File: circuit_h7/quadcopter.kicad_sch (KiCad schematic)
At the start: 143 parts, among them J1 Conn_01x01_Female, J10 Conn_01x01_Female, J11 Conn_01x04_Male, J12 Conn_01x04_Male, J13 Conn_01x01_Female, J14 Conn_01x01_Female, J15 Conn_01x01_Female, J16 Conn_01x01_Female, J17 Conn_01x01_Female, J18 USB_C_Receptacle_USB2.0, J19 Conn_01x08_Male, J2 Conn_01x01_Female, J20 Conn_01x01_Female, J21 Conn_01x01_Female, J22 Conn_01x01_Female, J23 Conn_01x01_Female, J24 Conn_01x01_Female, J25 Conn_01x01_Female, J26 Conn_01x01_Female, J28 Conn_01x01_Female, J29 Conn_01x01_Female, J3 Conn_01x01_Female, J30 Conn_01x01_Female, J31 Conn_01x01_Female, J32 Conn_01x01_Female, J33 Conn_01x01_Female, J37 Conn_01x01_Female, J4 Conn_01x01_Female, J40 Conn_01x01_Female, J41 Conn_01x01_Female, J42 Conn_01x01_Female, J43 Conn_01x01_Female, J44 Conn_01x01_Female, J45 Conn_01x01_Female, J47 Conn_01x01_Female, J48 Conn_01x01_Female, J49 Conn_01x01_Female, J5 Conn_Coaxial, J50 Conn_01x01_Female, J6 Conn_01x06_Male, J7 Conn_01x01_Female, J8 Conn_01x01_Female, J9 Conn_01x01_Female, Q1 AO3400A, SW1 SW_DIP_x01, U1 STM32H723VGH6, U10 ESP8285, U11 AMS1117-5.0, U12 TPS5430DDA, U13 5v, 3A, U2 ICM-42605, U3 DPS310, U4 3V3, U5 EUP3458 1.2A, 30V max input, 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, U6 2450FM07D0034T, U7 W25Q80DVUXIE TR (16M), U8 SX1281, U9 5v, 500mA, Y1 16M, Y2 52Mhz, 12pF, Y3 40M

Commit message: More work on H7 board
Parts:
- removed C21: 10nF 50V, Capacitor_SMD:C_0402_1005Metric, symbol Device:C
- removed C22: 2.2u, Capacitor_SMD:C_0402_1005Metric, symbol Device:C
- removed C24: 47uF 16V, Capacitor_SMD:C_1210_3225Metric, symbol Device:C
- removed C27: 22u 35v, Capacitor_SMD:C_0805_2012Metric, symbol Device:C
- removed C42: 150p, Capacitor_SMD:C_0402_1005Metric, symbol Device:C
- removed C43: 100n, Capacitor_SMD:C_0402_1005Metric, symbol Device:C
- removed C44: 1.5n, Capacitor_SMD:C_0402_1005Metric, symbol Device:C
- removed C45, C46: 10u, Capacitor_SMD:C_0805_2012Metric, symbol Device:C
- removed D2: 40v 1A B5819WS, Diode_SMD:D_SOD-323, symbol Device:D
- removed L4: 22u 900mA, Anyleaf_Shared:SMNR4020 inductor, symbol Device:L
- removed R17: 300, Resistor_SMD:R_0402_1005Metric, symbol Device:R
- removed R19: 10k, Resistor_SMD:R_0402_1005Metric, symbol Device:R
- removed U11: AMS1117-5.0, Package_TO_SOT_SMD:SOT-223-3_TabPin2, symbol Regulator_Linear:AMS1117-5.0
- removed U13: 5v, 3A, Package_DFN_QFN:DFN-10-1EP_3x3mm_P0.5mm_EP1.65x2.38mm, symbol water_monitor-rescue:MCP1802-3.3-Anyleaf_shared
- removed U5: EUP3458 1.2A, 30V max input, adj output, Package_TO_SOT_SMD:TSOT-23-6, symbol Regulator_Switching:AAT1217ICA-1.2
- removed U9: 5v, 500mA, Package_TO_SOT_SMD:TSOT-23-5, symbol water_monitor-rescue:MCP1802-3.3-Anyleaf_shared
- added J27, J34, J35, J36: Conn_01x01_Female, TestPoint:TestPoint_Pad_1.0x1.0mm, symbol Connector:Conn_01x01_Female
- added U5: MT2492 600kHz 16v 2A, Package_TO_SOT_SMD:SOT-23-6, symbol Regulator_Switching:TPS5430DDA
- C14: value 10uF 50V -> 22uF 25v; LCSC C440198 -> C602037; now in the parts list
- C15: value 1u 50V -> 22n; footprint Capacitor_SMD:C_0603_1608Metric -> Capacitor_SMD:C_0402_1005Metric; LCSC C15849 -> C1532; now in the parts list
- C20: value 47uF 16V -> 100uF 6.3V; footprint Capacitor_SMD:C_1210_3225Metric -> Capacitor_SMD:C_1206_3216Metric; LCSC C412625 -> C15008; now in the parts list
- J12: now left out of the parts list
- J3, J31, J37: footprint TestPoint:TestPoint_Pad_1.5x1.5mm -> TestPoint:TestPoint_Pad_2.0x2.0mm
- L2: value 100u 450mA -> 10u 2A; footprint Anyleaf_Shared:SMNR4020 inductor -> Inductor_SMD:L_Taiyo-Yuden_MD-4040; LCSC C467068 -> C98364; now in the parts list
- R10: value 3.3K -> 1.4k; LCSC C25890 -> C39650
- R11: value 300 -> 13k; footprint Resistor_SMD:R_0402_1005Metric -> Resistor_SMD:R_0603_1608Metric; LCSC C25102 -> C22797
- R7: value 3.3K -> 10k; LCSC C25890 -> C25744; now in the parts list
- R8: value 300 -> 100k; LCSC C25102 -> C25741; now in the parts list
- U12: value TPS5430DDA -> TPS5430DDA 3A 36v
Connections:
- net +10V: now also C14.2, U5.4 (EN), U5.5 (VIN); no longer C20.1
- net +BATT: no longer C14.2
- net GND: now also J27.1 (Pin_1), U5.2 (GND); no longer C15.1, J12.1 (Pin_1), R8.1
- net NRST: now also J36.1 (Pin_1); no longer J12.4 (Pin_4)
- net SWCLK: now also J35.1 (Pin_1); no longer J12.3 (Pin_3)
- net SWDIO: now also J34.1 (Pin_1); no longer J12.2 (Pin_2)
- net ELRS_LED: now reaches R9.2, U10.8 (XPD_DCDC)
- net at U12.4 (VSENSE): now also R10.2, R7.1; no longer R11.2
- net at D5.2 (A): now also C20.1, L2.2, R8.2
- net at L2.1: now also C15.2, U5.6 (SW)
- new net: C15.1, U5.1 (BS)
- new net: R11.2, R8.1, U5.3 (FB)
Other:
- note added: "10v - 5v regulator"
- note added: "See DS for info on selecting passives (5v reg)"
- note added: "These passives (for the 10v reg)chosen based on an official interactive TI tool. Screenshot of results included in folder."
- note added: "battery - 10v regulator"
- note added: "todo: Consider 1-2 10uF caps here (1206 likely)"
- note added: "todo: Is a 1A diode here good enough?"
- note added: "todo: consider 22uH here"
- note removed: "3.3k and 300 lead to 9.6V output"
- note removed: "Calculated inductor value, for 25.2v in, 9.6vout, 30% ripple, and 1A current: 16.5uH"
- note removed: "Todo: 1A may not be enough. 2A should be"
- note removed: "Todo: Sort out passives on this 5v reg"
- note removed: "V_out = 0.8V * (R1 + R2)/R2"
- note removed: "extended part. Basic v is 1206"
- note removed: "todo: Find part for this 10ju cap"
- note removed: "todo: Non-extended part for this 1.5n cap?"
- moved on the sheet: C38, C39, C40, C41, D7, H1, H2, H3, H4, J12, L5, R10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

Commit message: More work on fusion
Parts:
- added J38: Conn_01x01_Female, TestPoint:TestPoint_Pad_1.0x1.0mm, symbol Connector:Conn_01x01_Female
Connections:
- net +10V: now also U5.1 (BS), U5.3 (FB); no longer U5.4 (EN), U5.5 (VIN)
- net GND: no longer U5.2 (GND)
- net ELRS_BOOT: now reaches U10.15 (GPIO0)
- net ELRS_BOOT: now also J38.1 (Pin_1)
- net at C15.1: now also U5.5 (VIN); no longer U5.1 (BS)
- net at R11.2, R8.1: now also U5.4 (EN); no longer U5.3 (FB)
- net at C15.2, L2.1: no longer U5.6 (SW)
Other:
- note added: "(Ground ELRS_BOOT to enable bootloader mode)"
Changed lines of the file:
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@@
   (junction (at 416.56 302.26) (diameter 0) (color 0 0 0 0)
   )
-  (junction (at 302.26 43.18) (diameter 0) (color 0 0 0 0)
-  )
   (junction (at 358.14 99.06) (diameter 0) (color 0 0 0 0)
   )
@@
     (stroke (width 0) (type default) (color 0 0 0 0))
   )
+  (wire (pts (xy 436.88 330.2) (xy 449.58 330.2))
+    (stroke (width 0) (type default) (color 0 0 0 0))
+  )
   (wire (pts (xy 279.4 375.92) (xy 281.94 375.92))
     (stroke (width 0) (type default) (color 0 0 0 0))
@@
     (effects (font (size 1.27 1.27)) (justify left bottom))
   )
+  (text "(Ground ELRS_BOOT to enable bootloader mode)" (at 457.2 330.2 0)
+    (effects (font (size 1.27 1.27)) (justify left bottom))
+  )
   (text "24-52Mhz crystal" (at 372.11 354.33 0)
     (effects (font (size 1.27 1.27)) (justify left bottom))
@@
     (effects (font (size 1.27 1.27)) (justify right bottom))
   )
+  (label "ELRS_BOOT" (at 436.88 330.2 0)
+    (effects (font (size 1.27 1.27)) (justify left bottom))
+  )
   (label "ELRS_BUSY" (at 48.26 297.18 180)
     (effects (font (size 1.27 1.27)) (justify right bottom))
@@
     (pin "2")
   )
-  (symbol (lib_name "TPS5430DDA_1") (lib_id "Regulator_Switching:TPS5430DDA") (at 304.8 33.02 0) (unit 1)
+  (symbol (lib_name "TPS5430DDA_1") (lib_id "Regulator_Switching:TPS5430DDA") (at 304.8 33.02 0) (mirror y) (unit 1)
     (in_bom yes) (on_board yes) (fields_autoplaced)
-    (property "Reference" "U5" (id 0) (at 304.8 21.59 0))
-    (property "Value" "MT2492 600kHz 16v 2A" (id 1) (at 304.8 24.13 0))
-    (property "Footprint" "Package_TO_SOT_SMD:SOT-23-6" (id 2) (at 306.07 41.91 0)
+    (property "Reference" "U5" (id 0) (at 304.8 20.32 0))
+    (property "Value" "MT2492 600kHz 16v 2A" (id 1) (at 304.8 22.86 0))
+    (property "Footprint" "Package_TO_SOT_SMD:SOT-23-6" (id 2) (at 303.53 41.91 0)
       (effects (font (size 1.27 1.27) italic) (justify left) hide)
     )
-    (property "Datasheet" "https://datasheet.lcsc.com/lcsc/1810262207_XI-AN-Aerosemi-Tech-MT2492_C89358.pdf" (id 3) (at 300.99 15.24 0)
+    (property "Datasheet" "https://datasheet.lcsc.com/lcsc/1810262207_XI-AN-Aerosemi-Tech-MT2492_C89358.pdf" (id 3) (at 308.61 15.24 0)
       (effects (font (size 1.27 1.27)) hide)
     )
@@
     (pin "1")
   )
+  (symbol (lib_id "Connector:Conn_01x01_Female") (at 454.66 330.2 0) (unit 1)
+    (in_bom no) (on_board yes)
+    (property "Reference" "J38" (id 0) (at 452.12 327.66 0)
+      (effects (font (size 1.27 1.27)) (justify left))
+    )
+    (property "Value" "Conn_01x01_Female" (id 1) (at 455.93 331.4699 0)
+      (effects (font (size 1.27 1.27)) (justify left) hide)
+    )
+    (property "Footprint" "TestPoint:TestPoint_Pad_1.0x1.0mm" (id 2) (at 454.66 330.2 0)
+      (effects (font (size 1.27 1.27)) hide)
+    )
+    (property "Datasheet" "~" (id 3) (at 454.66 330.2 0)
+      (effects (font (size 1.27 1.27)) hide)
+    )
+    (pin "1")
+  )
   (symbol (lib_id "power:GND") (at 58.42 200.66 90) (unit 1)
     (in_bom yes) (on_board yes)
@@
       (reference "J37") (unit 1) (value "Conn_01x01_Female") (footprint "TestPoint:TestPoint_Pad_2.0x2.0mm")
     )
+    (path "/eade017e-723d-44a4-bbbf-c52c84a30817"
+      (reference "J38") (unit 1) (value "Conn_01x01_Female") (footprint "TestPoint:TestPoint_Pad_1.0x1.0mm")
+    )
     (path "/0567dae1-cf2c-438a-99dc-8576c8bfdd09"

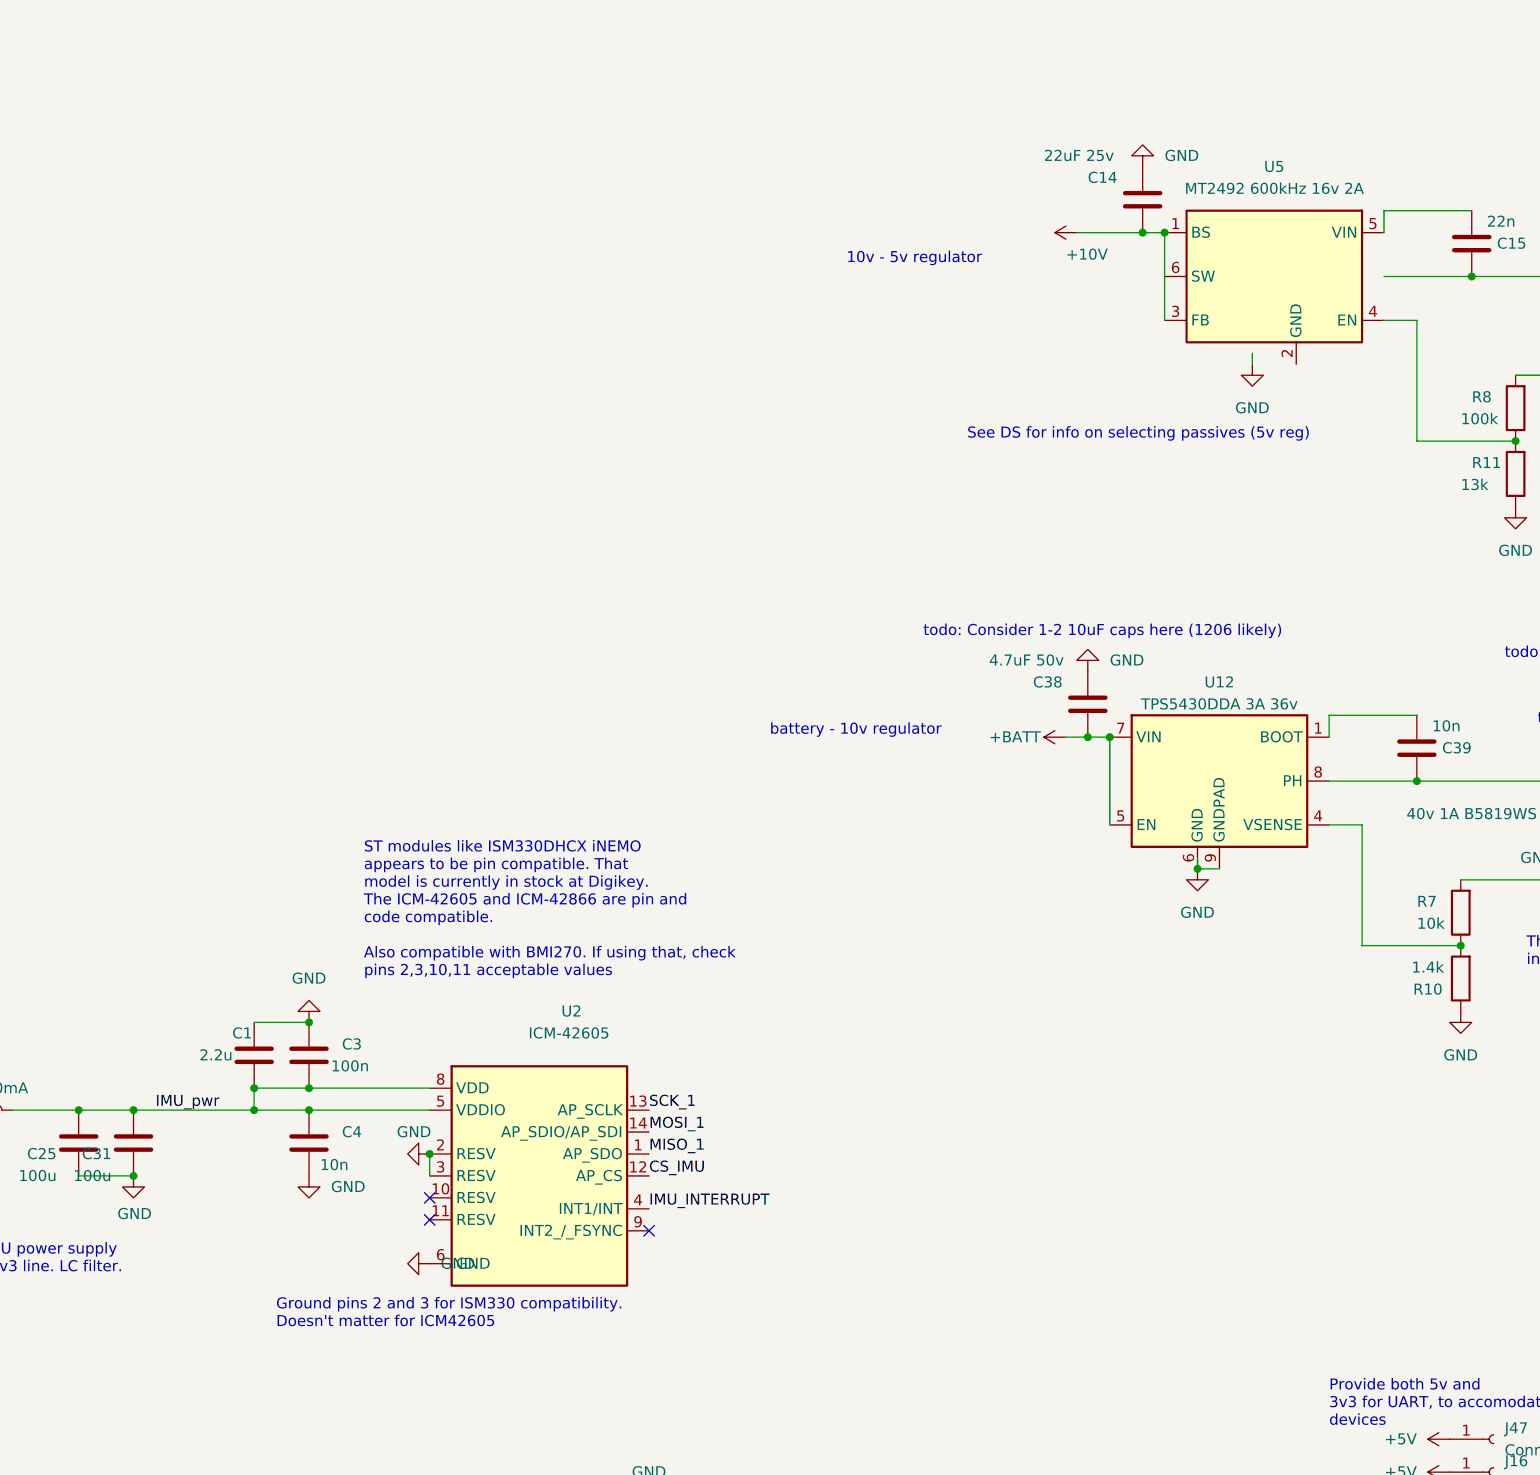
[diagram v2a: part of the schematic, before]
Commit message: Added timer ARR/PSC and clock config speeds for H743@480Mhz, H723 at 520 and 550Mhz
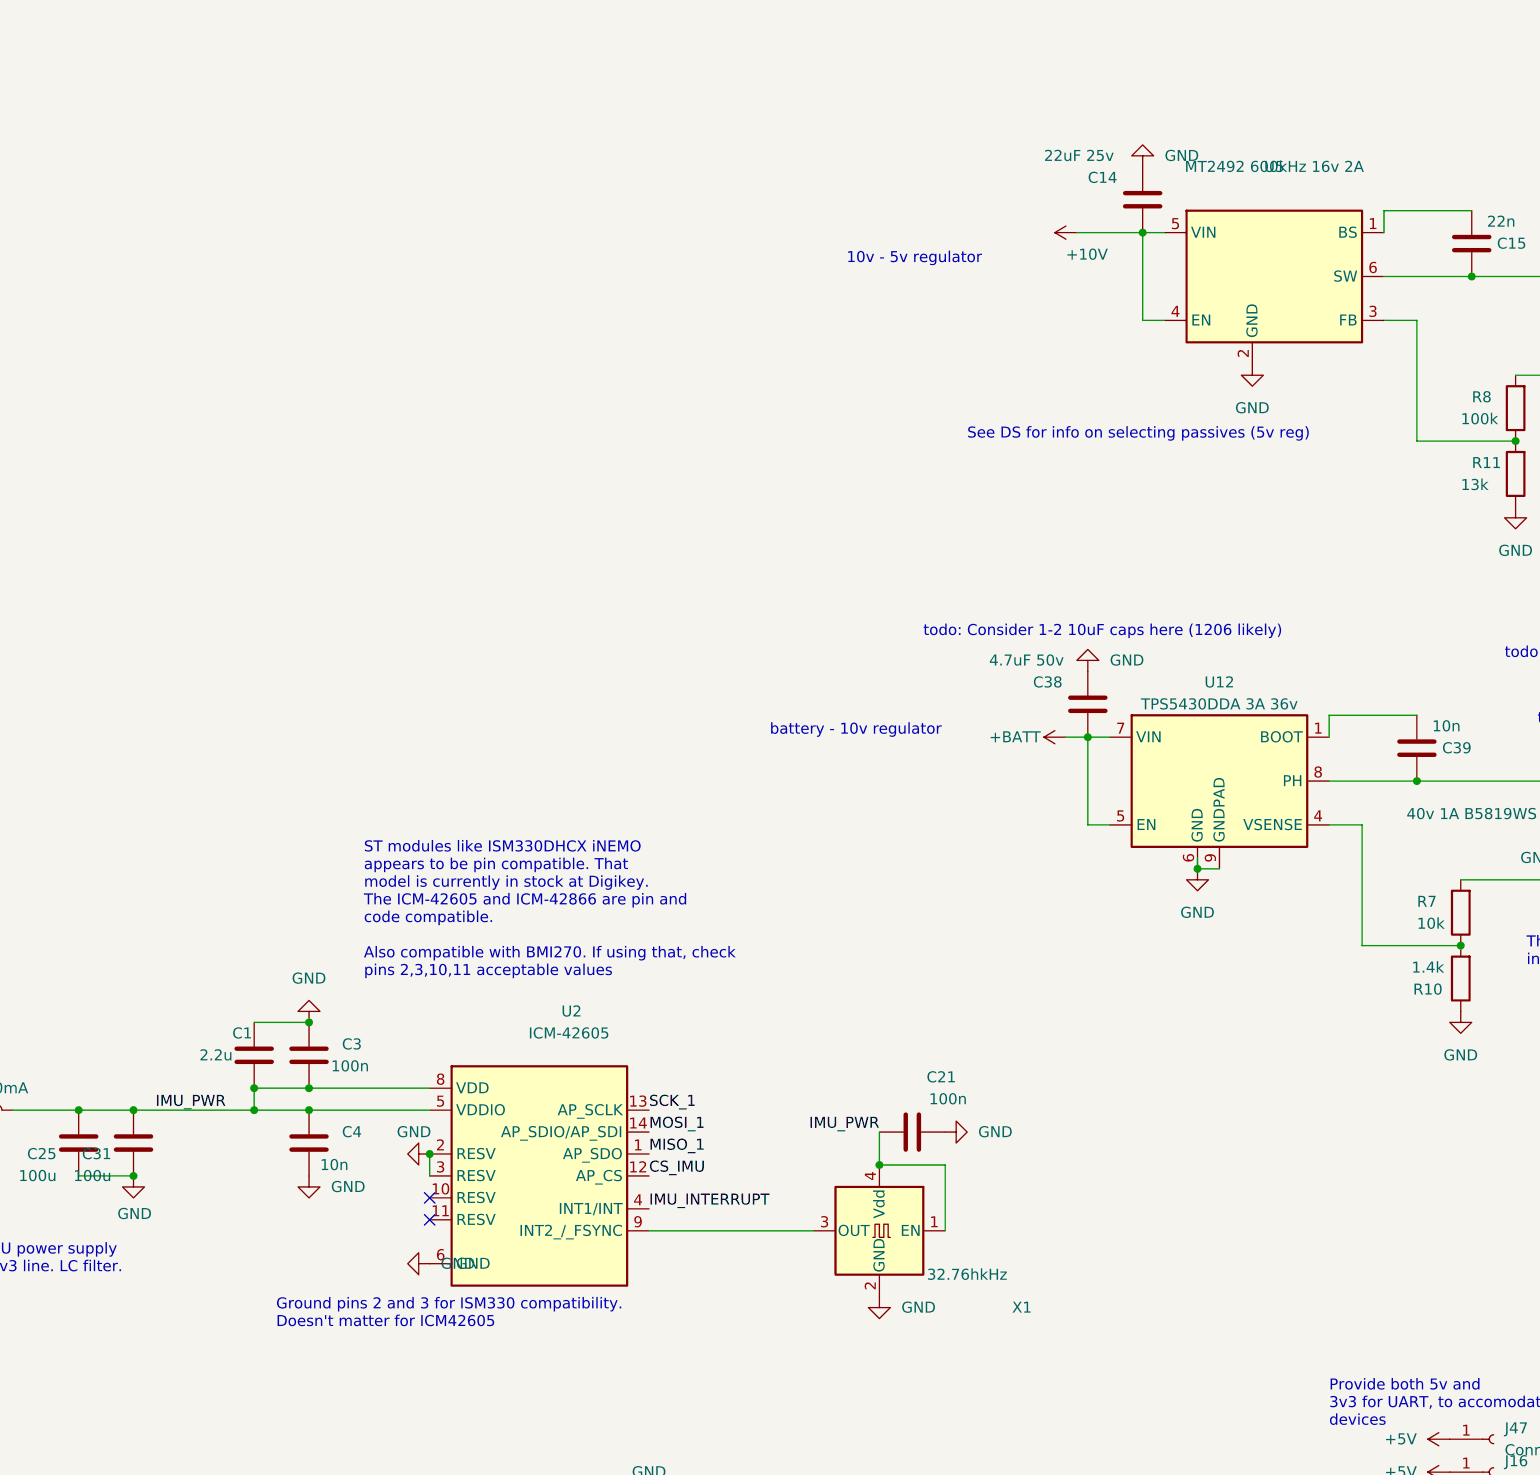
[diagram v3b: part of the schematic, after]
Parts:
- added C21: 100n, Capacitor_SMD:C_0402_1005Metric, symbol Device:C
- added X1: 32.76hkHz, Oscillator:Oscillator_SMD_EuroQuartz_XO32-4Pin_3.2x2.5mm, symbol Oscillator:TXC-7C
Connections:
- net +10V: now also U5.4 (EN), U5.5 (VIN); no longer U5.1 (BS), U5.3 (FB)
- net GND: now also U5.2 (GND), C21.2, X1.2 (GND)
- net at U2.9 (INT2_/_FSYNC): now also X1.3 (OUT)
- net at R11.2, R8.1: now also U5.3 (FB); no longer U5.4 (EN)
- net at C15.1: now also U5.1 (BS); no longer U5.5 (VIN)
- net at U5.6 (SW): now also C15.2, L2.1
- net IMU_pwr renamed IMU_PWR
- net IMU_PWR: now also C21.1, X1.1 (EN), X1.4 (Vdd)
- no-connect marks 11 -> 10
